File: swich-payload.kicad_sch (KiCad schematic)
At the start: 2 parts, among them P1 USB_C_Plug_USB2.0, U1 CH554E

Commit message: usb + memory
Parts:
- added BT1: Battery_Cell, symbol Device:Battery_Cell
- added U3: AT25SF161B-SSHB-T, SOIC8_8S1_REN, symbol AT25SF161B:AT25SF161B-SSHB-T
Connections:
- net at P1.A1 (GND), P1.A12 (GND), P1.B1 (GND)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: now also BT1.2 (-), U3.4 (GND)
- net at P1.A4 (VBUS), P1.A9 (VBUS), P1.B4 (VBUS)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: no longer U1.9 (VCC/VDD)
- net at P1.A5 (CC): now also U1.1 (P1.4/T2_/CAP1_/SCS/TIN2/UCC1/AIN1)
- net at U1.10 (V33): now also BT1.1 (+), U3.8 (VCC)
- net at U1.2 (P1.5/MOSI/PWM1/TIN3/UCC2/AIN2): now also U3.5 (SI(IO0))
- net at U1.3 (P1.6/MISO/RXD1/TIN4): now also U3.2 (SO(IO1))
- net at U1.4 (P1.7/SCK/TXD1/TIN5): now also U3.6 (SCK)
- no-connect marks 1 -> 0
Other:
- moved on the sheet: U1

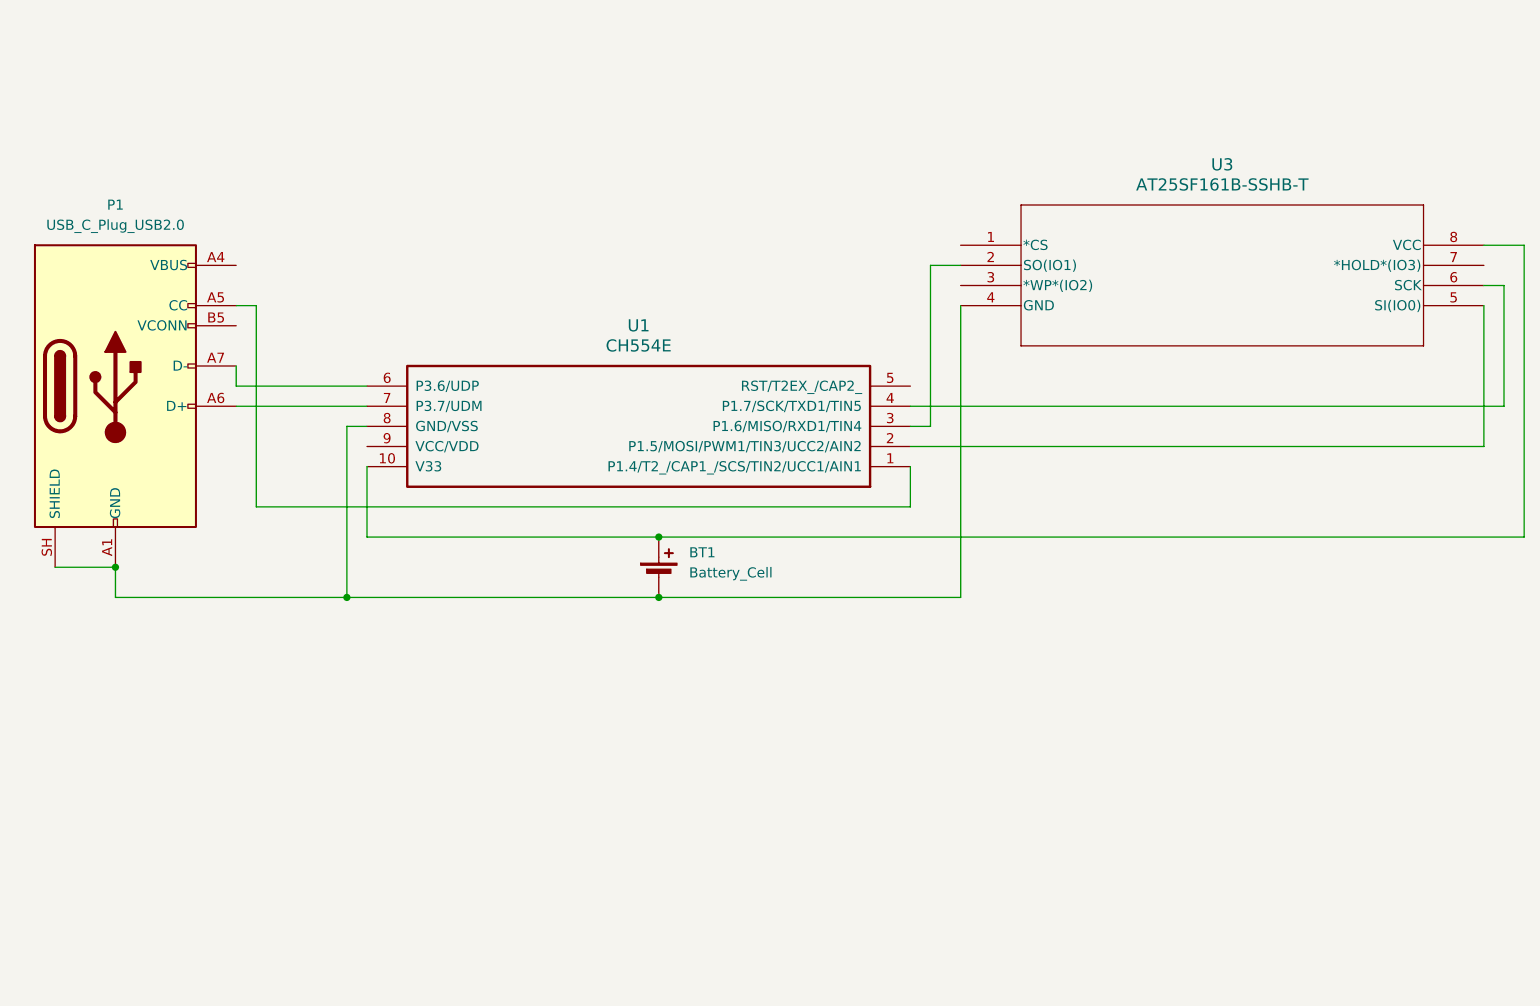
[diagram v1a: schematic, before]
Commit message: qffn
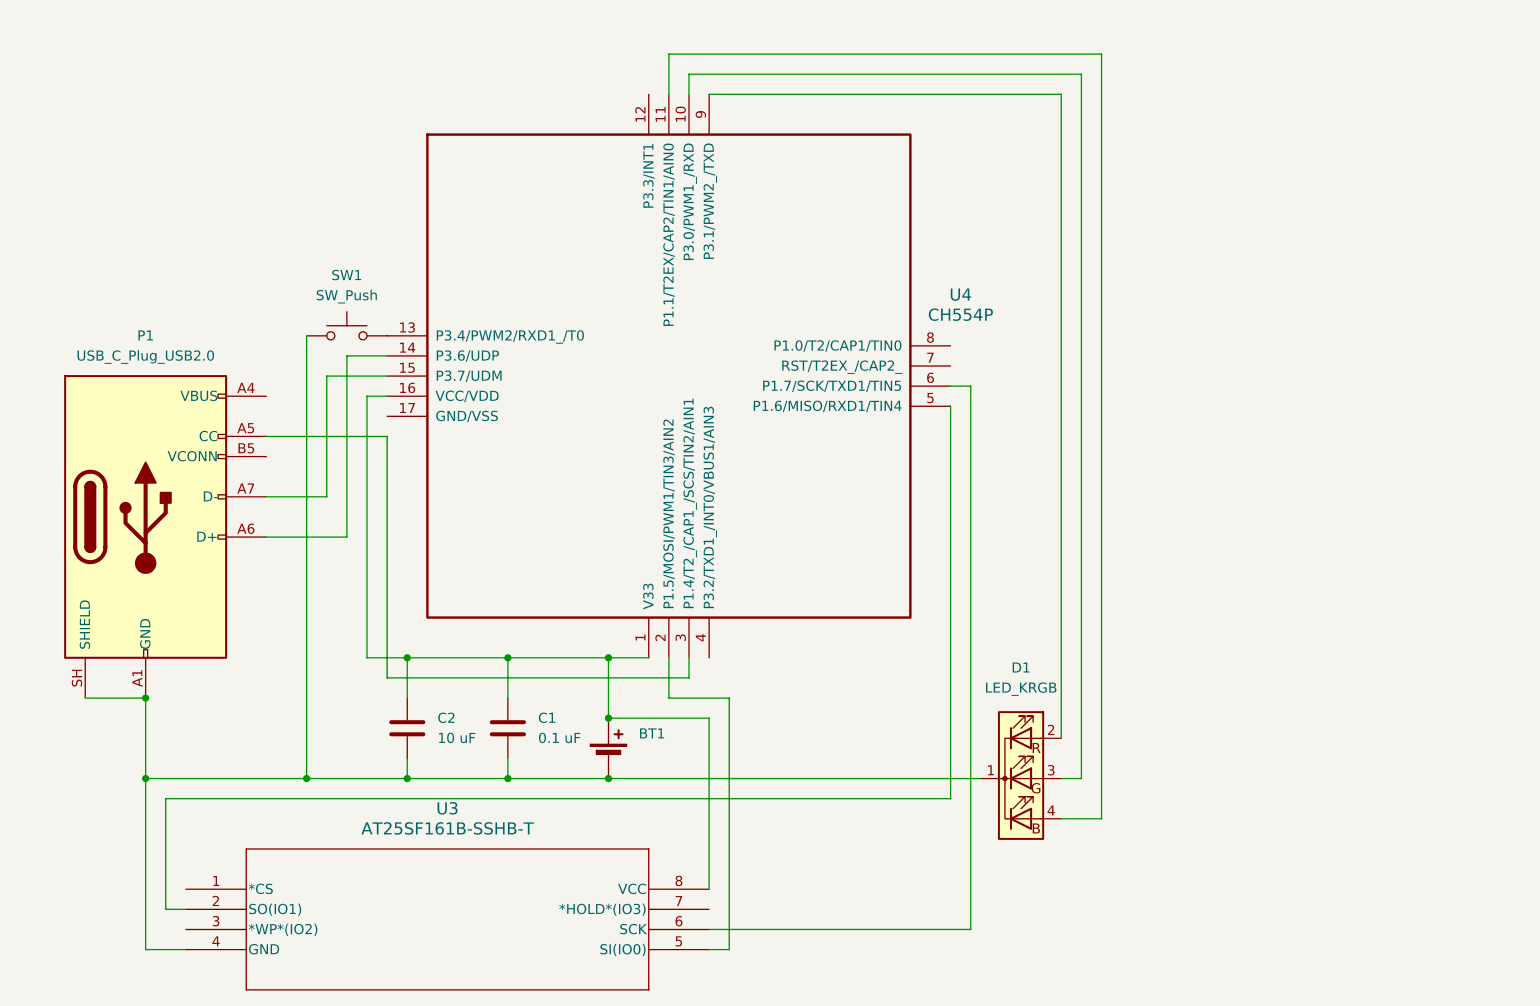
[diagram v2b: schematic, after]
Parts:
- removed U1: CH554E, Package_SO:MSOP-10_3x3mm_P0.5mm, symbol wch:CH554E
- added C1: 0.1 uF, symbol Device:C
- added C2: 10 uF, symbol Device:C
- added D1: LED_KRGB, symbol Device:LED_KRGB
- added SW1: SW_Push, symbol Switch:SW_Push
- added U4: CH554P, Package_DFN_QFN:QFN-16-1EP_3x3mm_P0.5mm_EP1.9x1.9mm, symbol wch:CH554P
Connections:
- net at BT1.2 (-), P1.A1 (GND), P1.A12 (GND)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: now also C1.2, C2.2, D1.1 (K), SW1.1
- net at P1.A5 (CC): now also U4.3 (P1.4/T2_/CAP1_/SCS/TIN2/AIN1)
- net at P1.A6 (D+): now also U4.14 (P3.6/UDP)
- net at P1.A7 (D-): now also U4.15 (P3.7/UDM)
- net at BT1.1 (+), U3.8 (VCC): now also C1.1, C2.1, U4.1 (V33), U4.16 (VCC/VDD)
- net at U3.5 (SI(IO0)): now also U4.2 (P1.5/MOSI/PWM1/TIN3/AIN2)
- net at U3.2 (SO(IO1)): now also U4.5 (P1.6/MISO/RXD1/TIN4)
- net at U3.6 (SCK): now also U4.6 (P1.7/SCK/TXD1/TIN5)
- new net: D1.2 (RA), U4.9 (P3.1/PWM2_/TXD)
- new net: D1.3 (GA), U4.10 (P3.0/PWM1_/RXD)
- new net: D1.4 (BA), U4.11 (P1.1/T2EX/CAP2/TIN1/AIN0)
- new net: SW1.2, U4.13 (P3.4/PWM2/RXD1_/T0)
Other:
- moved on the sheet: BT1, P1, U3

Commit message: qffn2
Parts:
- removed U3: AT25SF161B-SSHB-T, SOIC8_8S1_REN, symbol AT25SF161B:AT25SF161B-SSHB-T
- removed U4: CH554P, Package_DFN_QFN:QFN-16-1EP_3x3mm_P0.5mm_EP1.9x1.9mm, symbol wch:CH554P
- added U1: AT25SF161B-SSHD-T, EasyEDA:SOIC-8_L4.9-W3.9-P1.27-LS6.0-BL, symbol EasyEDA:AT25SF161B-SSHD-T
- added U2: CH554P, Package_DFN_QFN:QFN-16-1EP_3x3mm_P0.5mm_EP1.9x1.9mm, symbol wch:CH554P
- BT1: footprint (none) -> EasyEDA:BAT-SMD_BHSD-2032-SM
- P1: footprint (none) -> EasyEDA:USB-SMD_TC-002_1
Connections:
- net GND: now reaches BT1.2 (-), C1.2, C2.2, D1.1 (K), P1.A1 (GND), P1.A12 (GND), P1.B1 (GND), P1.B12 (GND), P1.SH (SHIELD)
- net GND: now also SW1.2, U1.4 (GND), U2.17 (GND/VSS); no longer SW1.1
- net USB CC: now reaches P1.A5 (CC)
- net USB CC: now also U2.3 (P1.4/T2_/CAP1_/SCS/TIN2/AIN1)
- net USB D+: now reaches P1.A6 (D+)
- net USB D+: now also U2.14 (P3.6/UDP)
- net USB D-: now reaches P1.A7 (D-)
- net USB D-: now also U2.15 (P3.7/UDM)
- net VCC: now reaches BT1.1 (+), C1.1, C2.1
- net VCC: now also U1.8 (VCC), U2.1 (V33), U2.16 (VCC/VDD)
- net RBG R: now reaches D1.2 (RA)
- net RBG R: now also U2.9 (P3.1/PWM2_/TXD)
- net RGB G: now reaches D1.3 (GA)
- net RGB G: now also U2.10 (P3.0/PWM1_/RXD)
- net RGB B: now reaches D1.4 (BA)
- net RGB B: now also U2.11 (P1.1/T2EX/CAP2/TIN1/AIN0)
- new net BUTTON: SW1.1, U2.13 (P3.4/PWM2/RXD1_/T0)
- new net CS: U1.1 (~{CS}), U2.8 (P1.0/T2/CAP1/TIN0)
- new net SCK: U1.6 (SCK), U2.6 (P1.7/SCK/TXD1/TIN5)
- new net SI: U1.5 (SI), U2.2 (P1.5/MOSI/PWM1/TIN3/AIN2)
- new net SO: U1.2 (SO), U2.5 (P1.6/MISO/RXD1/TIN4)
- no-connect marks 0 -> 7
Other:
- title: (none) -> Switch Payload Injector
- moved on the sheet: BT1, C1, C2

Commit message: final
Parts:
- removed D1: LED_KRGB, symbol Device:LED_KRGB
- removed SW1: SW_Push, symbol Switch:SW_Push
- removed U1: AT25SF161B-SSHD-T, EasyEDA:SOIC-8_L4.9-W3.9-P1.27-LS6.0-BL, symbol EasyEDA:AT25SF161B-SSHD-T
- added JP1: SolderJumper_2_Open, Jumper:SolderJumper-2_P1.3mm_Open_Pad1.0x1.5mm, symbol Jumper:SolderJumper_2_Open
- added SW2: SW_Push, EasyEDA:SW-SMD_L3.0-W2.5-P3.40-LS4.0-EH, symbol Switch:SW_Push
- added SW3: TS6635PA 250GF TACTILE SWITCH, EasyEDA:SW-SMD_4P-L6.4-W6.3-P4.00-LS9.5, symbol EasyEDA:TS6635PA250GFTACTILESWITCH
- added TP1, TP2, TP6, TP7, TP8: TestPoint_Square, TestPoint:TestPoint_Pad_D2.0mm, symbol Connector:TestPoint_Square
- added TP3, TP5: TestPoint_Square, TestPoint:TestPoint_Pad_D1.0mm, symbol Connector:TestPoint_Square
- added U3: GL-1615RGB01-B, EasyEDA:LED-SMD_4P-L1.6-W1.5-BL-C9900013097, symbol EasyEDA:GL-1615RGB01-B
- added U4: ZD25WD20CTIGT, EasyEDA:SOP-8_L4.9-W3.9-P1.27-LS6.0-BL, symbol EasyEDA:ZD25WD20CTIGT
- C1, C2: footprint (none) -> Capacitor_SMD:C_0805_2012Metric
- P1: footprint EasyEDA:USB-SMD_TC-002_1 -> EasyEDA:USB-C-SMD_TYPE-C-31-G-10
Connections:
- net BUTTON: now also SW3.1
- net CS: now also TP5.1, U4.1 (~{CS})
- net GND: now also SW3.3, SW3.4, TP2.1, U3.2, U4.4 (VSS)
- net RBG R: now also U3.1
- net RGB B: now also U3.3
- net RGB G: now also U3.4
- net SCK: now also TP6.1, U4.6 (SCLK)
- net SI: now also TP8.1, U4.5 (SI/IO0)
- net SO: now also TP7.1, U4.2 (SO/IO1)
- net USB CC: now also TP3.1
- net VCC: now also JP1.1 (A), SW2.2, TP1.1, U4.8 (VCC); no longer U2.1 (V33)
- net RST: now reaches U2.7 (RST/T2EX_/CAP2_)
- net RST: now also SW2.1
- new net: JP1.2 (B), U2.1 (V33)
